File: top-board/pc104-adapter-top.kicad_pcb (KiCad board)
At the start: 4 copper layers, 86.1 x 91.8 mm, 16 parts, among them J1 Conn_01x13_Male, J10 SAMTEC-SSW-126-01-G-D, J2 Conn_01x13_Male, J3 Conn_01x13_Male, J4 Conn_01x13_Male, J5 Conn_01x13_Male, J6 Conn_01x13_Male, J7 Conn_01x13_Male, J8 Conn_01x13_Male, J9 SAMTEC-SSW-126-01-G-D

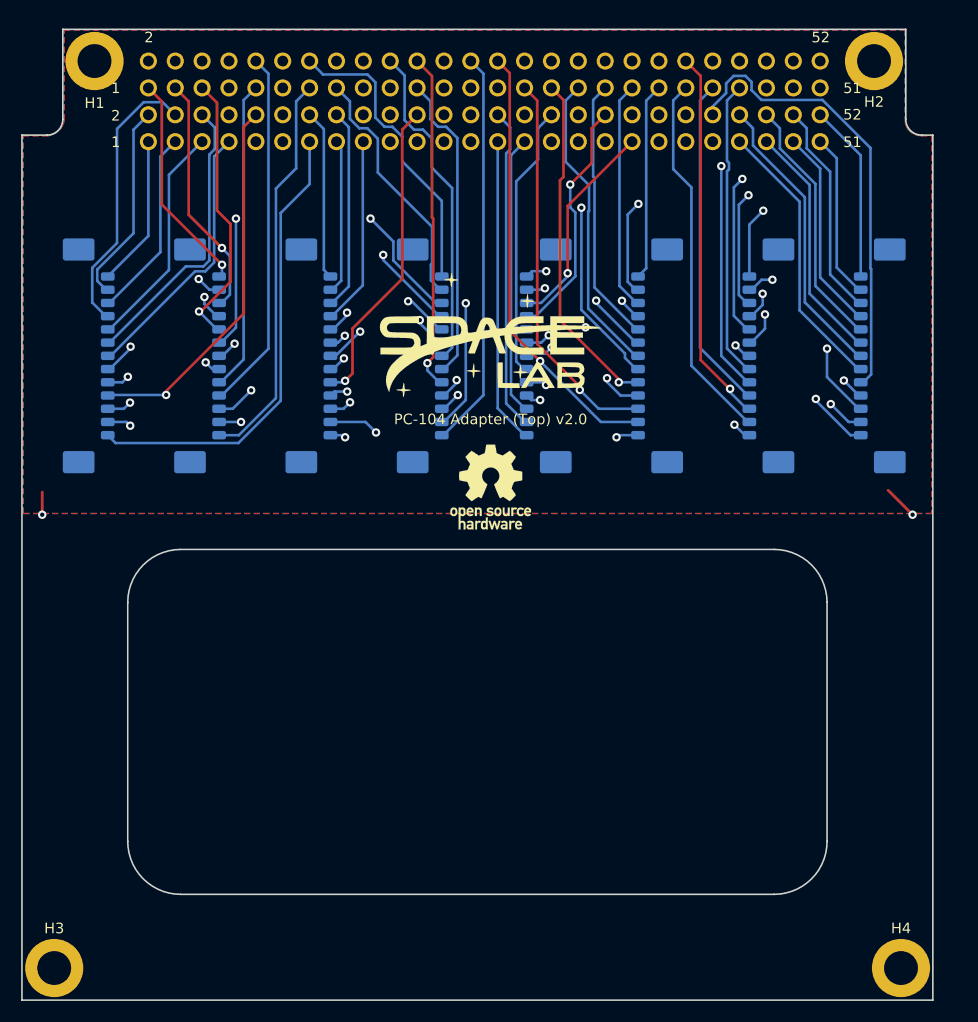
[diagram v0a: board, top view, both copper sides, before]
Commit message: top-board: Updating the board shape and fixing the screw holes positions #14
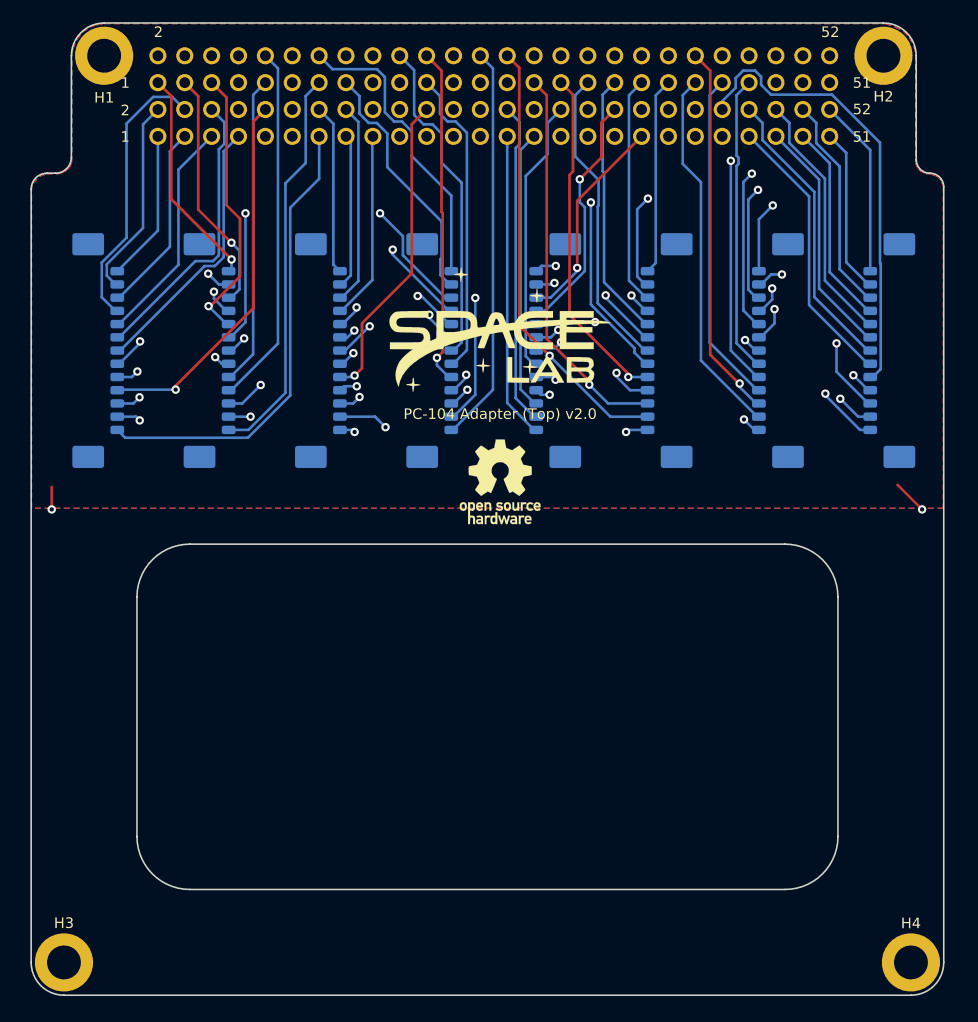
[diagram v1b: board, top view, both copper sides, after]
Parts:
- moved H4 1.05 mm to (186.3, 140.4)
- moved H3 1.05 mm to (106.3, 140.4)
- moved H1 1.04 mm to (110.1, 54.6)
- moved G*** 1.03 mm to (147.5, 80.5)
- moved J10 1.03 mm to (146.9, 61.0)
- moved J3 1.03 mm to (162.7, 82.5)
- moved J4 1.03 mm to (173.2, 82.5)
- moved J5 1.03 mm to (110.1, 82.5)
- moved J6 1.03 mm to (131.1, 82.5)
- moved J8 1.03 mm to (183.7, 82.5)
- moved J9 1.03 mm to (146.9, 55.9)
- moved REF** 1.03 mm to (147.5, 94.9)
- moved J1 1.03 mm to (120.6, 82.5)
- moved J2 1.03 mm to (141.6, 82.5)
- moved J7 1.03 mm to (152.2, 82.5)
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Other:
- board size 86.1 x 91.8 mm -> 86.3 x 91.9 mm

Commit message: top-board: Fixing mounting holes position and general improvements
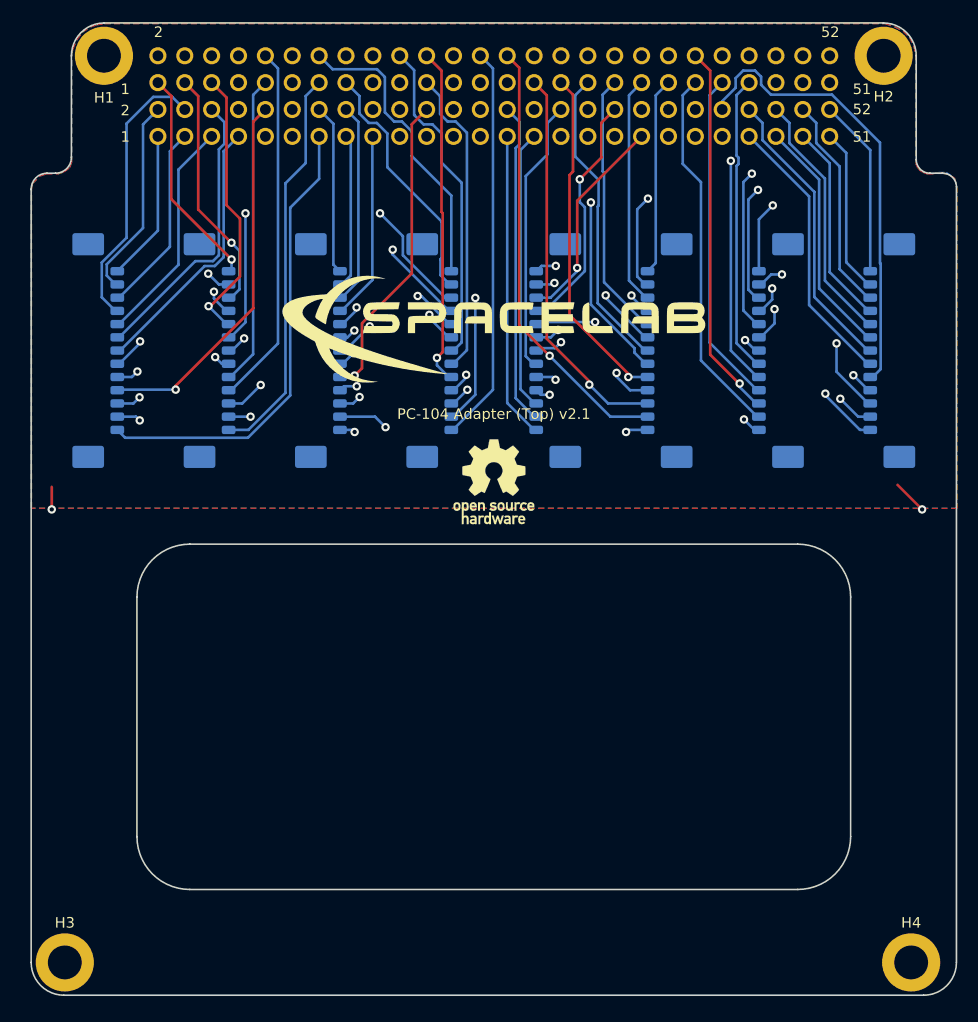
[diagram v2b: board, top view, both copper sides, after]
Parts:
- removed the G*** at (147.5, 80.5)
- added G***: LOGO, lib:spacelab-logo, F.Cu at (146.9, 80.5)
- moved REF** 0.60 mm to (146.9, 94.9)
- moved H3 0.09 mm to (106.3, 140.3)
- moved H4 0.06 mm to (186.3, 140.3)
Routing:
- net GND: track 92.0 -> 93.2 mm
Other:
- board size 86.3 x 91.9 mm -> 87.5 x 91.9 mm
- net class Default removed
- board text added: "PC-104 Adapter (Top) v2.1"
- board text removed: "PC-104 Adapter (Top) v2.0"
